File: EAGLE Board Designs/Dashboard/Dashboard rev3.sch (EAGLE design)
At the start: 91 parts, among them J2 CONNECTOR-8_NF_S_RA_BLACK, J3 CONNECTOR-CAN_NF_S_RA_BLACK, J4 CONNECTOR-AVR-ISP_2X05_SMD_, K1 CPC1002N, Q1 TRANSISTOR_N_MOS__PMV15ENEA, Q2 TRANSISTOR_N_MOS__PMV15ENEA, Q3 TRANSISTOR_N_MOS__PMV15ENEA, Q4 TRANSISTOR_N_MOS__PMV15ENEA, Q5 TRANSISTOR_N_MOS__PMV15ENEA, Q6 TRANSISTOR_N_MOS__PMV15ENEA, U1 ATMEGA328P-AU, U2 TCAN1051HQV-Q1, U3 MCP2515, U4 MCP23S17, U5 CONVERTER_DC/DC_12V-5V, U6 RE46C100, X1 CRYSTAL16MHZ, X2 CRYSTAL16MHZ, X7 CONNECTOR-8NANO-FIT_RIGHT_ANG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

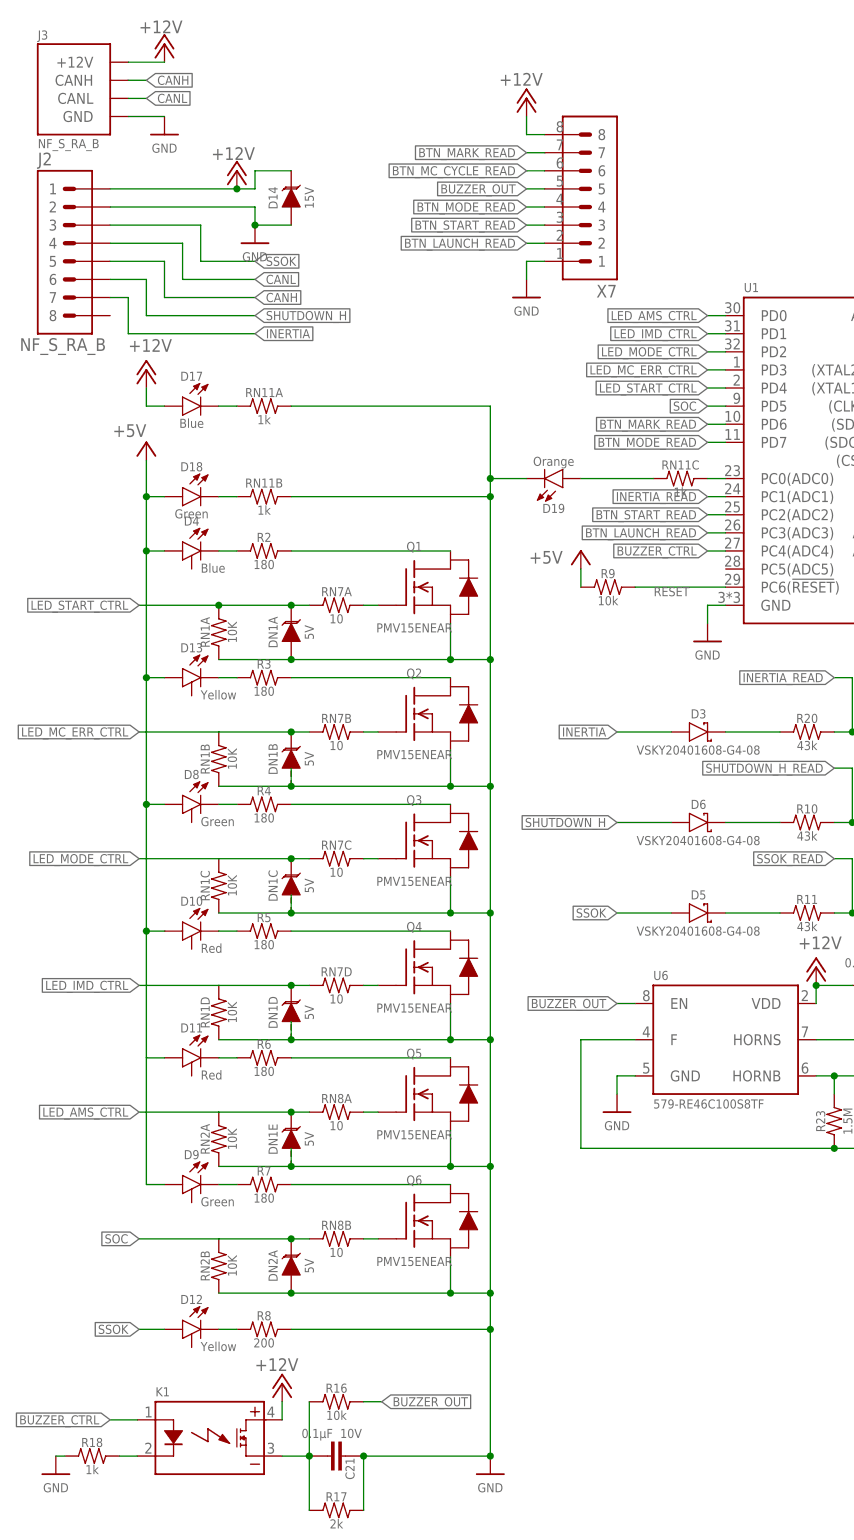
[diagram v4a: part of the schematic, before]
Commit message: Worked on placement and removed buzzer out from signals
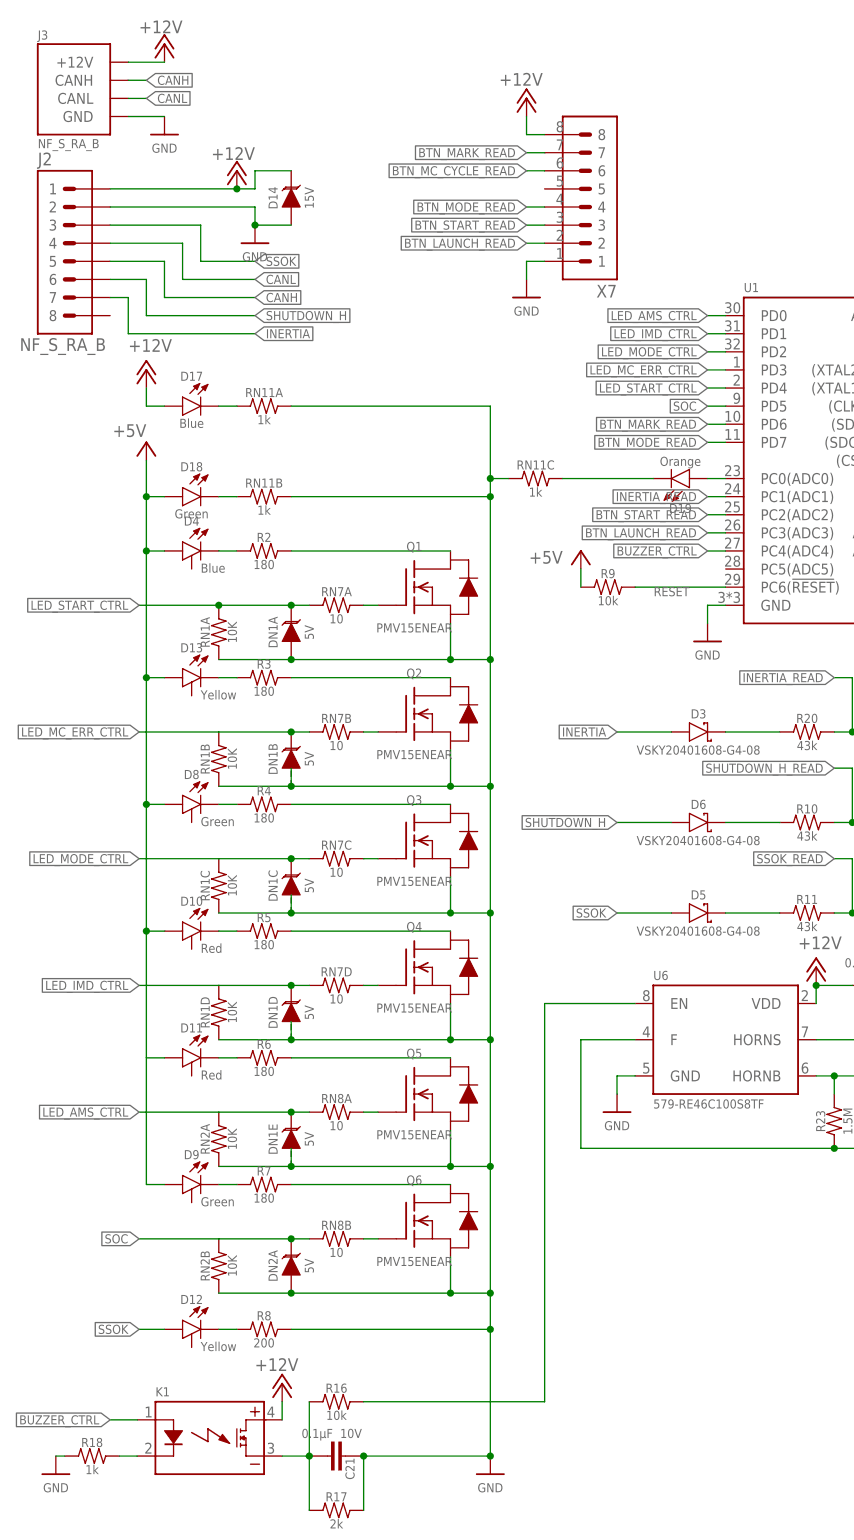
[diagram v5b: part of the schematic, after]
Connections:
- removed net N$22: U6.EN
- removed net N$64: RN11C.2, U1.PC0(ADC0)
- removed net N$67: D19.A, RN11C.1
- new net N$43: D19.C, RN11C.2
- new net N$44: D19.A, U1.PC0(ADC0)
- net BUZZER_OUT: no longer X7.5
- net GND: now also RN11C.1; no longer D19.C
- net N$41: now also U6.EN
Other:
- moved on the sheet: D19, RN11C
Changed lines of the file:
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@@
 <attribute name="NAME" x="31.75" y="148.336" size="1.27" layer="96" align="bottom-center"/>
 </instance>
-<instance part="D19" gate="LED" x="81.28" y="147.32" smashed="yes" rot="R180">
-<attribute name="COLOR" x="82.55" y="149.098" size="1.27" layer="95" rot="R180" align="top-center"/>
-<attribute name="NAME" x="82.55" y="143.764" size="1.27" layer="96" rot="R180" align="bottom-center"/>
+<instance part="D19" gate="LED" x="99.06" y="147.32" smashed="yes" rot="R180">
+<attribute name="COLOR" x="100.33" y="149.098" size="1.27" layer="95" rot="R180" align="top-center"/>
+<attribute name="NAME" x="100.33" y="143.764" size="1.27" layer="96" rot="R180" align="bottom-center"/>
 </instance>
 <instance part="RN11" gate="A" x="43.18" y="157.48" smashed="yes">
@@
 <attribute name="RESISTANCE" x="41.91" y="143.51" size="1.27" layer="96" align="top-center"/>
 </instance>
-<instance part="RN11" gate="C" x="101.6" y="147.32" smashed="yes">
-<attribute name="NAME" x="100.33" y="148.59" size="1.27" layer="95" align="bottom-center"/>
-<attribute name="RESISTANCE" x="100.33" y="146.05" size="1.27" layer="96" align="top-center"/>
+<instance part="RN11" gate="C" x="81.28" y="147.32" smashed="yes">
+<attribute name="NAME" x="80.01" y="148.59" size="1.27" layer="95" align="bottom-center"/>
+<attribute name="RESISTANCE" x="80.01" y="146.05" size="1.27" layer="96" align="top-center"/>
 </instance>
 <instance part="P+9" gate="1" x="44.45" y="20.32" smashed="yes">
@@
 <pinref part="RN11" gate="A" pin="2"/>
 <pinref part="RN11" gate="B" pin="2"/>
-<pinref part="D19" gate="LED" pin="C"/>
+<pinref part="C21" gate="G$1" pin="2"/>
 <wire x1="73.66" y1="147.32" x2="73.66" y2="144.78" width="0.1524" layer="91"/>
-<wire x1="78.74" y1="147.32" x2="73.66" y2="147.32" width="0.1524" layer="91"/>
-<junction x="73.66" y="147.32"/>
-<pinref part="C21" gate="G$1" pin="2"/>
 <wire x1="55.88" y1="10.16" x2="55.88" y2="2.54" width="0.1524" layer="91"/>
 <pinref part="R17" gate="G$1" pin="2"/>
@@
 <junction x="73.66" y="10.16"/>
 <junction x="55.88" y="10.16"/>
+<pinref part="RN11" gate="C" pin="1"/>
+<wire x1="76.2" y1="147.32" x2="73.66" y2="147.32" width="0.1524" layer="91"/>
+<junction x="73.66" y="147.32"/>
 </segment>
 <segment>
@@
 <junction x="40.64" y="182.88"/>
 <pinref part="J2" gate="G$1" pin="2"/>
-</segment>
-<segment>
-<wire x1="22.86" y1="198.12" x2="27.94" y2="198.12" width="0.1524" layer="91"/>
-<pinref part="P17" gate="1" pin="GND"/>
-<pinref part="J3" gate="G$1" pin="GND"/>
 </segment>
 <segment>
@@
 <pinref part="P24" gate="1" pin="GND"/>
 <wire x1="132.08" y1="76.2" x2="132.08" y2="73.66" width="0.1524" layer="91"/>
+</segment>
+<segment>
+<pinref part="P17" gate="1" pin="GND"/>
+<pinref part="J3" gate="G$1" pin="GND"/>
+<wire x1="27.94" y1="198.12" x2="22.86" y2="198.12" width="0.1524" layer="91"/>
 </segment>
 </net>
@@
 </segment>
 <segment>
-<pinref part="P+18" gate="1" pin="+12V"/>
-<wire x1="22.86" y1="205.74" x2="27.94" y2="205.74" width="0.1524" layer="91"/>
-<pinref part="J3" gate="G$1" pin="+12V"/>
-</segment>
-<segment>
 <pinref part="P+23" gate="1" pin="+12V"/>
 <wire x1="20.32" y1="187.96" x2="38.1" y2="187.96" width="0.1524" layer="91"/>
@@
 <wire x1="119.38" y1="76.2" x2="124.46" y2="76.2" width="0.1524" layer="91"/>
 <junction x="119.38" y="76.2"/>
+</segment>
+<segment>
+<pinref part="J3" gate="G$1" pin="+12V"/>
+<pinref part="P+18" gate="1" pin="+12V"/>
+<wire x1="22.86" y1="205.74" x2="27.94" y2="205.74" width="0.1524" layer="91"/>
 </segment>
 </net>
@@
 <net name="BUZZER_OUT" class="0">
 <segment>
-<wire x1="81.28" y1="187.96" x2="78.74" y2="187.96" width="0.1524" layer="91"/>
-<label x="78.74" y="187.96" size="1.27" layer="95" rot="R180" xref="yes"/>
-<pinref part="X7" gate="G$1" pin="5"/>
-</segment>
-<segment>
-<label x="58.42" y="17.78" size="1.27" layer="95" xref="yes"/>
 <pinref part="C21" gate="G$1" pin="1"/>
 <wire x1="48.26" y1="10.16" x2="48.26" y2="2.54" width="0.1524" layer="91"/>
@@
 <wire x1="44.45" y1="10.16" x2="48.26" y2="10.16" width="0.1524" layer="91"/>
 <junction x="48.26" y="10.16"/>
-<label x="91.44" y="73.66" size="1.27" layer="95" rot="R180" xref="yes"/>
 <pinref part="R16" gate="G$1" pin="1"/>
 <wire x1="48.26" y1="10.16" x2="48.26" y2="17.78" width="0.1524" layer="91"/>
@@
 </segment>
 </net>
-<net name="N$64" class="0">
-<segment>
-<pinref part="U1" gate="G$1" pin="PC0(ADC0)"/>
-<pinref part="RN11" gate="C" pin="2"/>
-<wire x1="106.68" y1="147.32" x2="104.14" y2="147.32" width="0.1524" layer="91"/>
-</segment>
-</net>
-<net name="N$67" class="0">
-<segment>
-<pinref part="RN11" gate="C" pin="1"/>
-<pinref part="D19" gate="LED" pin="A"/>
-<wire x1="96.52" y1="147.32" x2="86.36" y2="147.32" width="0.1524" layer="91"/>
-</segment>
-</net>
 <net name="N$70" class="0">
 <segment>
@@
 </segment>
 </net>
-<net name="N$22" class="0">
-<segment>
-<pinref part="U6" gate="G$1" pin="EN"/>
-<wire x1="93.98" y1="73.66" x2="91.44" y2="73.66" width="0.1524" layer="91"/>
-</segment>
-</net>
 <net name="N$28" class="0">
 <segment>
@@
 <segment>
 <pinref part="R16" gate="G$1" pin="2"/>
-<wire x1="55.88" y1="17.78" x2="58.42" y2="17.78" width="0.1524" layer="91"/>
-</segment>
-</net>
+<wire x1="55.88" y1="17.78" x2="81.28" y2="17.78" width="0.1524" layer="91"/>
+<wire x1="81.28" y1="17.78" x2="81.28" y2="73.66" width="0.1524" layer="91"/>
+<pinref part="U6" gate="G$1" pin="EN"/>
+<wire x1="81.28" y1="73.66" x2="93.98" y2="73.66" width="0.1524" layer="91"/>
+</segment>
+</net>
+<net name="N$43" class="0">
+<segment>
+<pinref part="RN11" gate="C" pin="2"/>
+<pinref part="D19" gate="LED" pin="C"/>
+<wire x1="96.52" y1="147.32" x2="83.82" y2="147.32" width="0.1524" layer="91"/>
+</segment>
+</net>
+<net name="N$44" class="0">
+<segment>
+<pinref part="D19" gate="LED" pin="A"/>
+<pinref part="U1" gate="G$1" pin="PC0(ADC0)"/>
+<wire x1="104.14" y1="147.32" x2="106.68" y2="147.32" width="0.1524" layer="91"/>
+</segment>
+</net>
